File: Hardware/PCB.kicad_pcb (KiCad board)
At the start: 2 copper layers, 53.4 x 22 mm, 11 parts, among them J1 Conn_01x04_Pin, U1 ME54BS01_V1.0, U2 MCP1700x-330xxTO

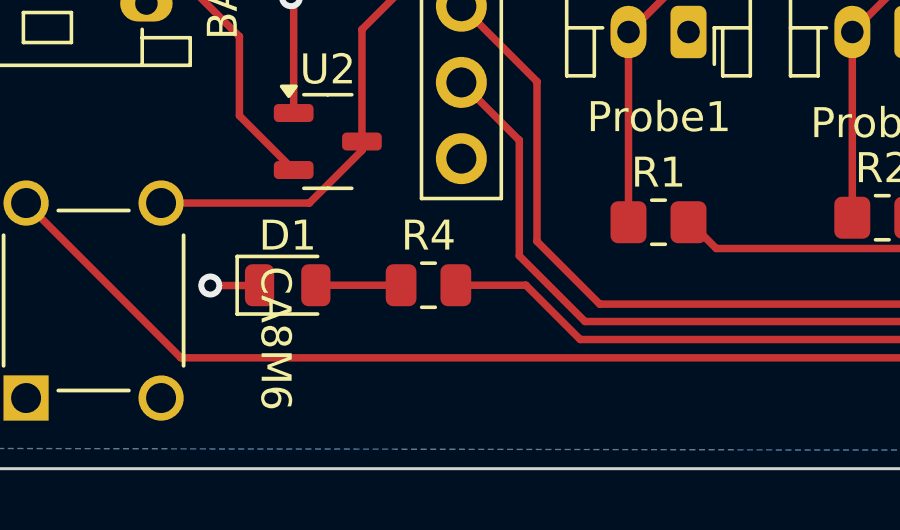
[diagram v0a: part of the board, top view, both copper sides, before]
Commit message: WIP Reworking schematic with Reddit feedback
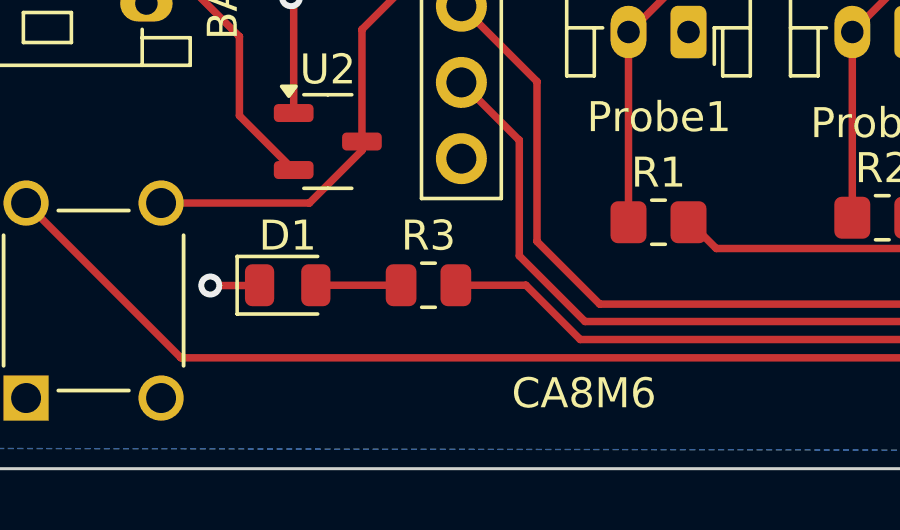
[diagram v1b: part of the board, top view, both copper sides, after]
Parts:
- renumbered R4 to R3
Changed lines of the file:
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@@
 	(paper "A4")
 	(title_block
-		(title "XIAO nRF52840 Dual Sensor")
-		(rev "4")
+		(title "Matter nRF54L15 Dual Temperature Sensor")
+		(rev "1")
 		(company "Cold Bear Ltd")
+		(comment 4 "AISLER Project ID: CJCXXZRD")
 	)
 	(layers
@@
 		(descr "Resistor SMD 0805 (2012 Metric), square (rectangular) end terminal, IPC_7351 nominal, (Body size source: IPC-SM-782 page 72, https://www.pcb-3d.com/wordpress/wp-content/uploads/ipc-sm-782a_amendment_1_and_2.pdf), generated with kicad-footprint-generator")
 		(tags "resistor")
-		(property "Reference" "R4"
+		(property "Reference" "R3"
 			(at 0 -1.65 0)
 			(layer "F.SilkS")
@@
 	)
 	(gr_text "CA8M6"
-		(at 51.68 75.34 270)
+		(at 64.96 75.34 0)
 		(layer "F.SilkS")
 		(effects

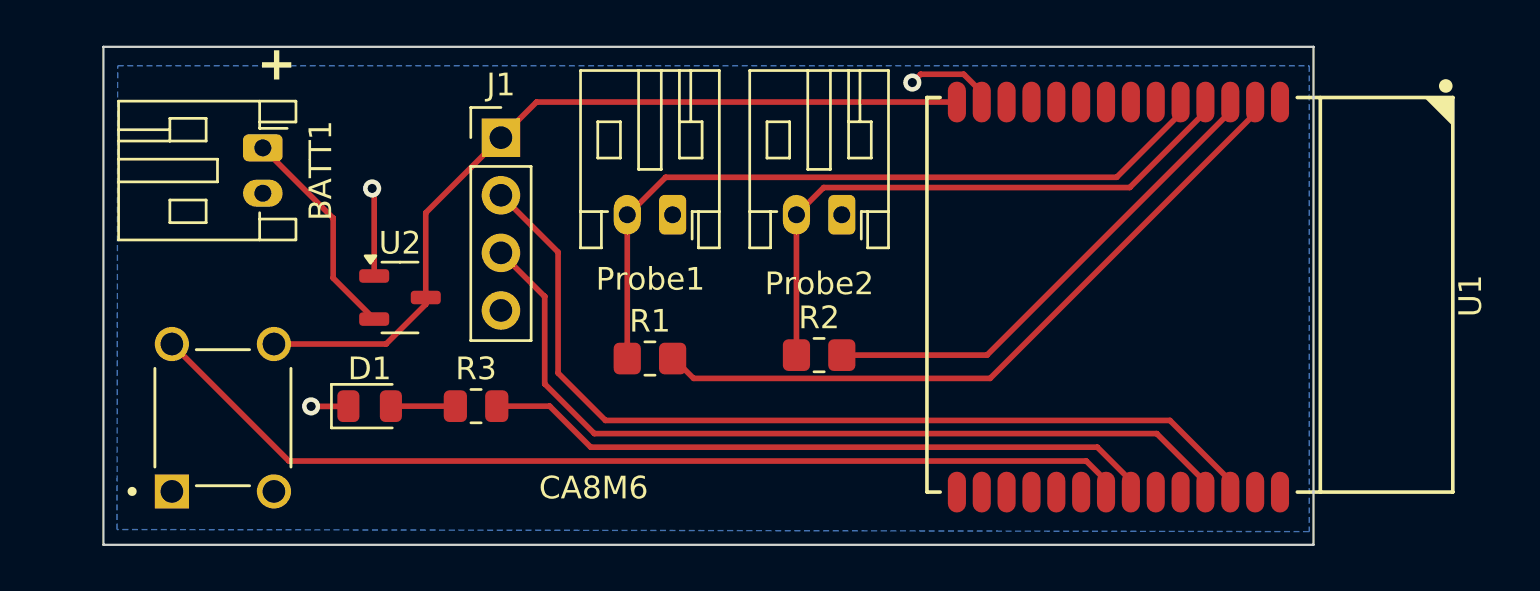
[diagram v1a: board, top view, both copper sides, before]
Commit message: Cleaned up schematic to be all in one. Trying to get updated layout for PCB
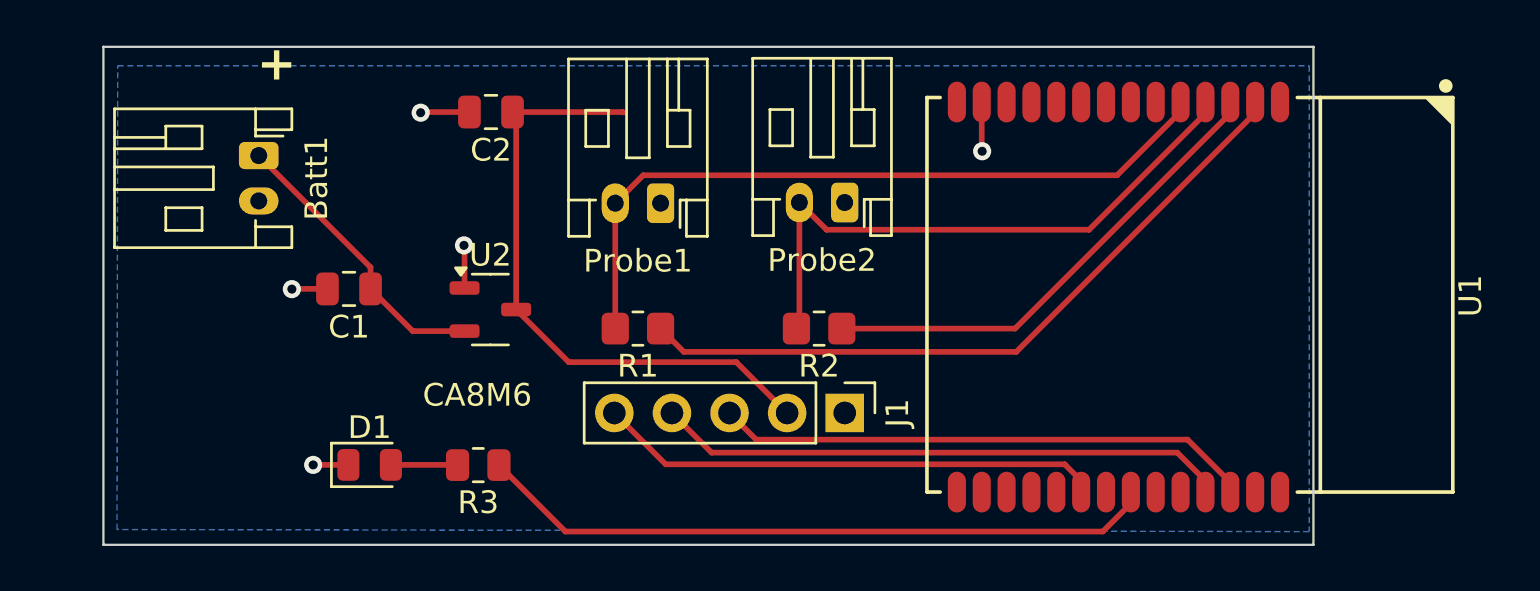
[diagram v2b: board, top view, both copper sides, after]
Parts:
- removed BATT1: Conn_01x02_Pin, Connector_JST:JST_PH_S2B-PH-K_1x02_P2.00mm_Horizontal
- removed S1: TS02-66-55-BK-100-LCR-D, TS02-66-55-BK-100-LCR-D:SW_TS02-66-55-BK-100-LCR-D
- added Batt1: Conn_01x02, Connector_JST:JST_PH_S2B-PH-K_1x02_P2.00mm_Horizontal, F.Cu at (47.8, 60.1)
- added C1: 1µF, Capacitor_SMD:C_0805_2012Metric, F.Cu at (51.8, 66.0)
- added C2: 1µF, Capacitor_SMD:C_0805_2012Metric, F.Cu at (58.0, 58.2)
- J1: value Conn_01x04_Pin -> Conn_01x05; footprint Connector_PinHeader_2.54mm:PinHeader_1x04_P2.54mm_Vertical -> Connector_PinHeader_2.54mm:PinHeader_1x05_P2.54mm_Vertical
- Probe1, Probe2: value Conn_01x02_Pin -> Conn_01x02
- R3: value R -> 50
- moved J1 19.4 mm to (73.6, 71.5), turned to -90 degrees
- moved U2 4.02 mm to (58.0, 66.9)
- moved R3 2.60 mm to (57.5, 73.8), turned to 180 degrees
- moved D1 2.59 mm to (52.7, 73.7)
- moved R1 1.42 mm to (64.5, 67.7), turned to 180 degrees
- moved R2 1.17 mm to (72.5, 67.7), turned to 180 degrees
- moved Probe1 0.74 mm to (65.5, 62.2)
- moved Probe2 0.56 mm to (73.6, 62.2)
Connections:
- J1 pad 1: /+3.3V -> GND
- J1 pad 2: /SWDCLK -> Net-(J1-Pin_2)
- J1 pad 3: /SWDIO -> Net-(J1-Pin_3)
- J1 pad 4: GND -> Net-(J1-Pin_4)
- Probe1 pad 2: /p1reading -> Net-(Probe1-Pin_2)
- Probe2 pad 2: /p2reading -> Net-(Probe2-Pin_2)
- R1 pad 1: /p1reading -> Net-(U1-P1.09)
- R1 pad 2: /dividerPower1 -> Net-(Probe1-Pin_2)
- R2 pad 1: /p2reading -> Net-(U1-P1.10)
- R2 pad 2: /dividerPower2 -> Net-(Probe2-Pin_2)
- R3 pad 1: Net-(D1-A) -> Net-(U1-P2.10)
- R3 pad 2: /indicator -> Net-(D1-A)
- U1 pad 14: /+3.3V -> Net-(J1-Pin_2)
- U1 pad 2: /dividerPower1 -> Net-(U1-P1.09)
- U1 pad 20: unconnected-(U1-NRESET-Pad20) -> Net-(J1-Pin_5)
- U1 pad 21: /reset -> Net-(U1-P2.09)
- U1 pad 22: /indicator -> Net-(U1-P2.10)
- U1 pad 25: /SWDIO -> Net-(J1-Pin_4)
- U1 pad 26: /SWDCLK -> Net-(J1-Pin_3)
- U1 pad 3: /dividerPower2 -> Net-(U1-P1.10)
- U1 pad 4: /p2reading -> Net-(Probe2-Pin_2)
- U1 pad 5: /p1reading -> Net-(Probe1-Pin_2)
- U2 pad 2: +BATT -> Net-(Batt1-Pin_1)
- U2 pad 3: /+3.3V -> Net-(J1-Pin_2)
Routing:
- net /reset: track 44.2 -> 0.00 mm
- net /SWDCLK: track 41.0 -> 0.00 mm
- net /SWDIO: track 38.4 -> 0.00 mm
- net /+3.3V: track 36.9 -> 0.00 mm
- net /p1reading: track 33.1 -> 0.00 mm
- net Net-(Probe1-Pin_2): track 0.00 -> 33.1 mm
- net Net-(U1-P1.09): track 0.00 -> 32.0 mm
- net /dividerPower1: track 31.3 -> 0.00 mm
- net Net-(U1-P2.10): track 0.00 -> 30.6 mm
- net /indicator: track 29.8 -> 0.00 mm
- net Net-(J1-Pin_2): track 0.00 -> 27.5 mm
- net Net-(Probe2-Pin_2): track 0.00 -> 26.6 mm
- net /p2reading: track 26.5 -> 0.00 mm
- net Net-(J1-Pin_4): track 0.00 -> 25.8 mm
- net Net-(J1-Pin_3): track 0.00 -> 24.3 mm
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
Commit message: Another PCB update
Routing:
- net Net-(J1-Pin_2): track 27.5 -> 42.4 mm
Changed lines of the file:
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@@
 	)
 	(segment
-		(start 59.13 66.89)
-		(end 61.447 69.207)
+		(start 69.04 69.41)
+		(end 71.08 71.45)
+		(width 0.25)
+		(layer "F.Cu")
+		(net 2)
+	)
+	(segment
+		(start 61.65 69.41)
+		(end 69.04 69.41)
 		(width 0.25)
 		(layer "F.Cu")
@@
 	)
 	(segment
-		(start 63.83 58.18)
-		(end 63.85 58.2)
-		(width 0.25)
-		(layer "F.Cu")
-		(net 2)
-	)
-	(segment
-		(start 58.97 58.18)
-		(end 63.83 58.18)
-		(width 0.25)
-		(layer "F.Cu")
-		(net 2)
-	)
-	(segment
 		(start 59.13 58.34)
 		(end 58.97 58.18)
@@
 	)
 	(segment
-		(start 68.837 69.207)
-		(end 71.08 71.45)
+		(start 59.13 66.89)
+		(end 61.65 69.41)
 		(width 0.25)
 		(layer "F.Cu")
@@
 	)
 	(segment
-		(start 61.447 69.207)
-		(end 68.837 69.207)
+		(start 78.566 57.74)
+		(end 59.41 57.74)
 		(width 0.25)
 		(layer "F.Cu")
+		(net 2)
+	)
+	(segment
+		(start 59.41 57.74)
+		(end 58.97 58.18)
+		(width 0.25)
+		(layer "F.Cu")

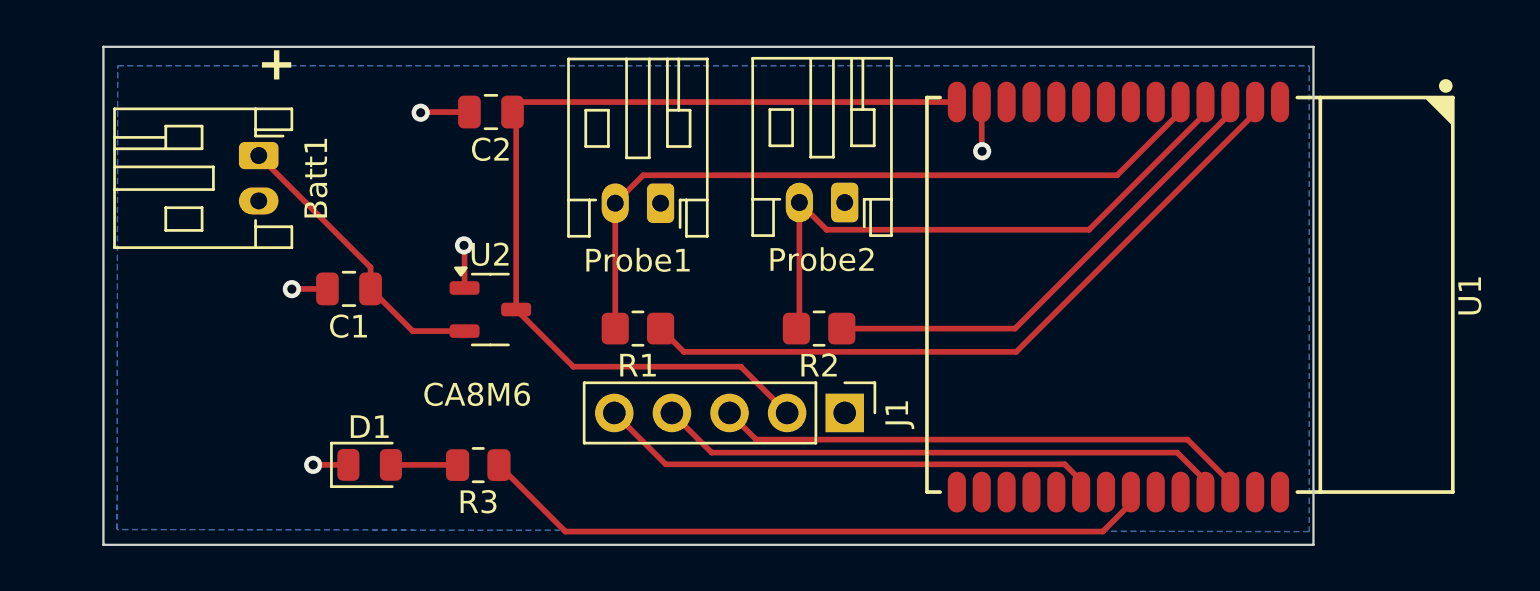
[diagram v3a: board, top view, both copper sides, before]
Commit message: PCB: Add another PIN to the header so power can be provided via J-Link.
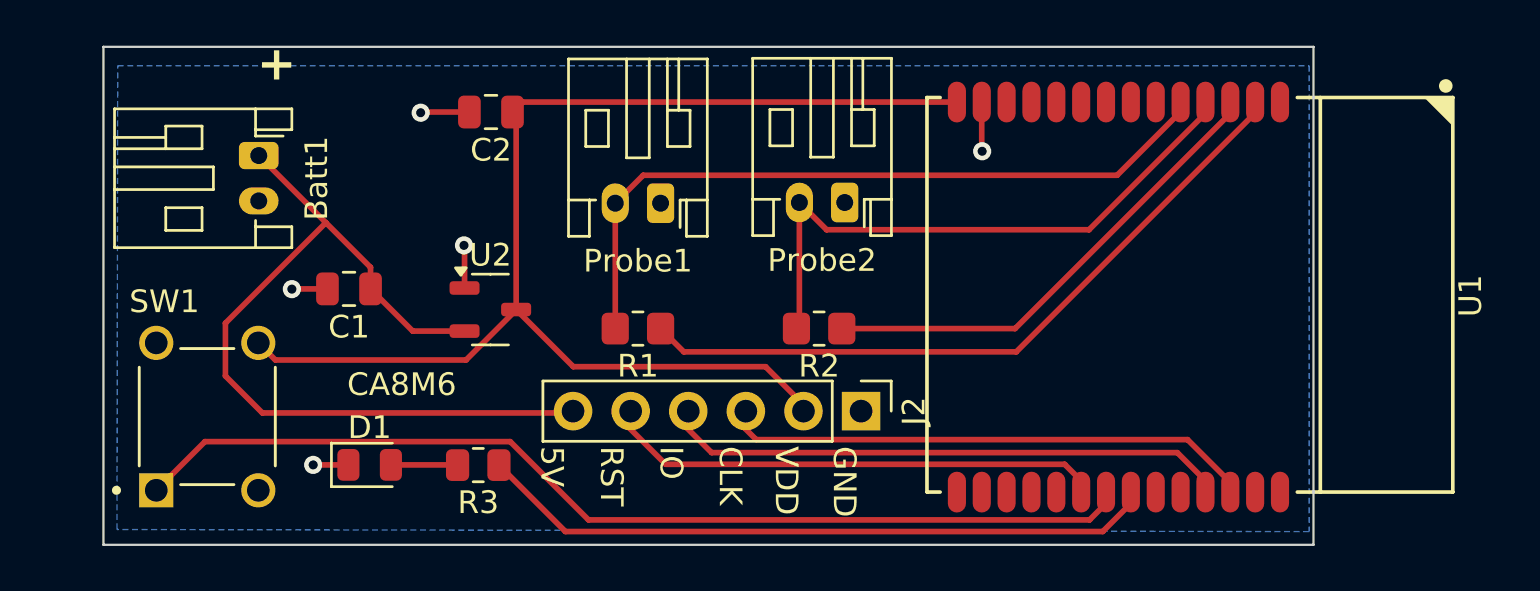
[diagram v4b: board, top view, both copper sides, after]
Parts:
- removed J1: Conn_01x05, Connector_PinHeader_2.54mm:PinHeader_1x05_P2.54mm_Vertical
- added J2: Conn_01x06, Connector_PinHeader_2.54mm:PinHeader_1x06_P2.54mm_Vertical, F.Cu at (74.3, 71.4)
- added SW1: SW_MEC_5E, TS02-66-55-BK-100-LCR-D:SW_TS02-66-55-BK-100-LCR-D, F.Cu at (45.5, 71.6)
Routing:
- net Net-(U1-P2.09): track 0.50 -> 45.5 mm
- net Net-(Batt1-Pin_1): track 12.8 -> 36.7 mm
- net Net-(J2-Pin_2): track 42.4 -> 55.9 mm
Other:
- board text added: "5V"
- board text added: "CLK"
- board text added: "GND"
- board text added: "IO"
- board text added: "RST"
- board text added: "VDD"

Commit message: Move decoupling capacitors closer to LDO. Ground module PIN 1.
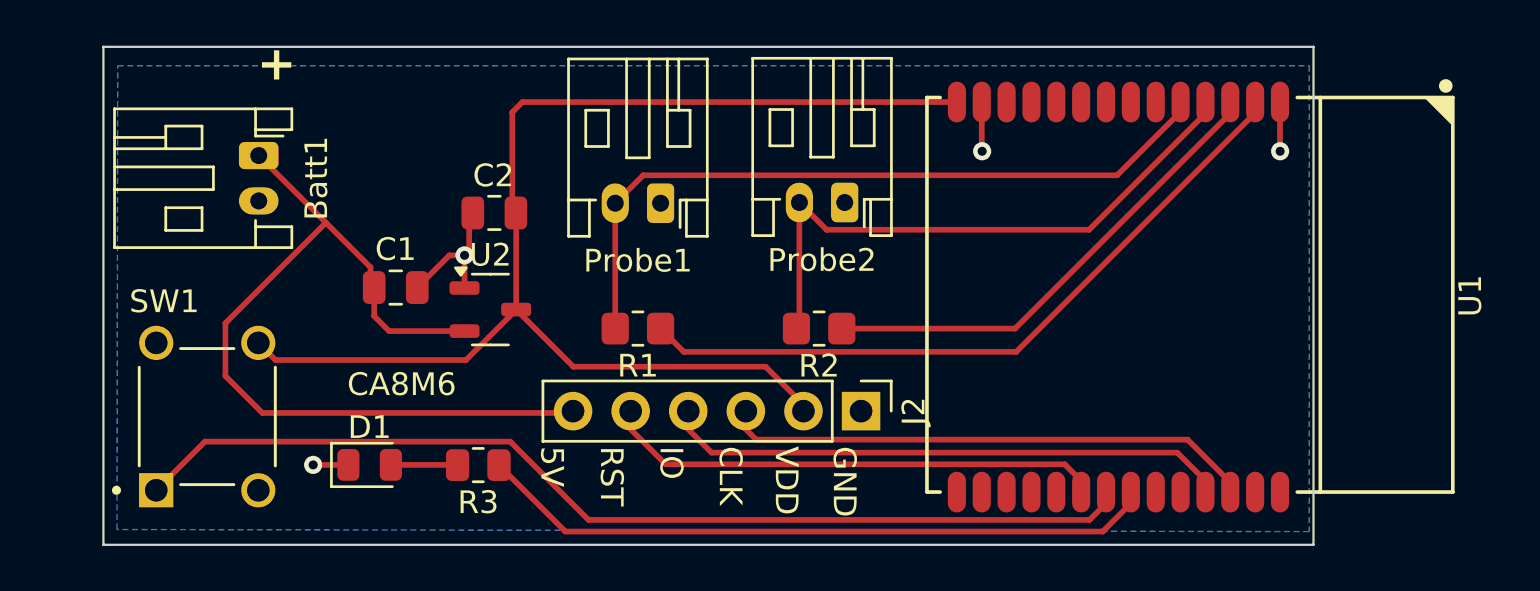
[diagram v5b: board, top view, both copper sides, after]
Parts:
- moved C2 4.45 mm to (58.2, 62.6)
- moved C1 2.06 mm to (53.8, 65.9), turned to 0 degrees
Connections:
- U1 pad 1: unconnected-(U1-GND-Pad1) -> GND
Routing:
- net GND: track 9.91 -> 12.6 mm, vias 5 -> 4
- net Net-(Batt1-Pin_1): track 36.7 -> 37.3 mm

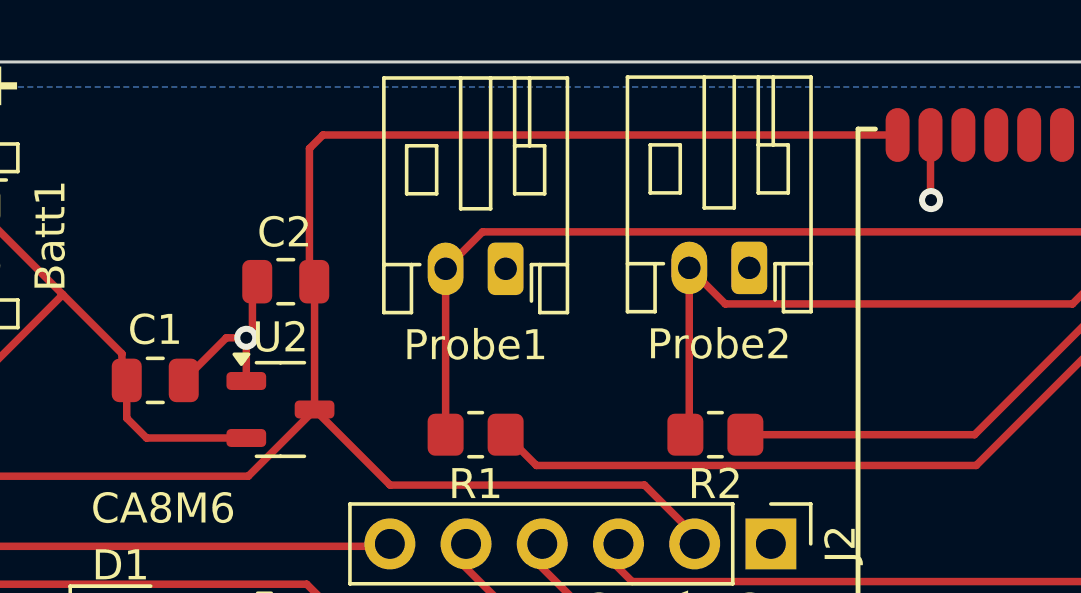
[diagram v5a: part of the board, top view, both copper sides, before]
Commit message: Move decoupling capacitors even closer
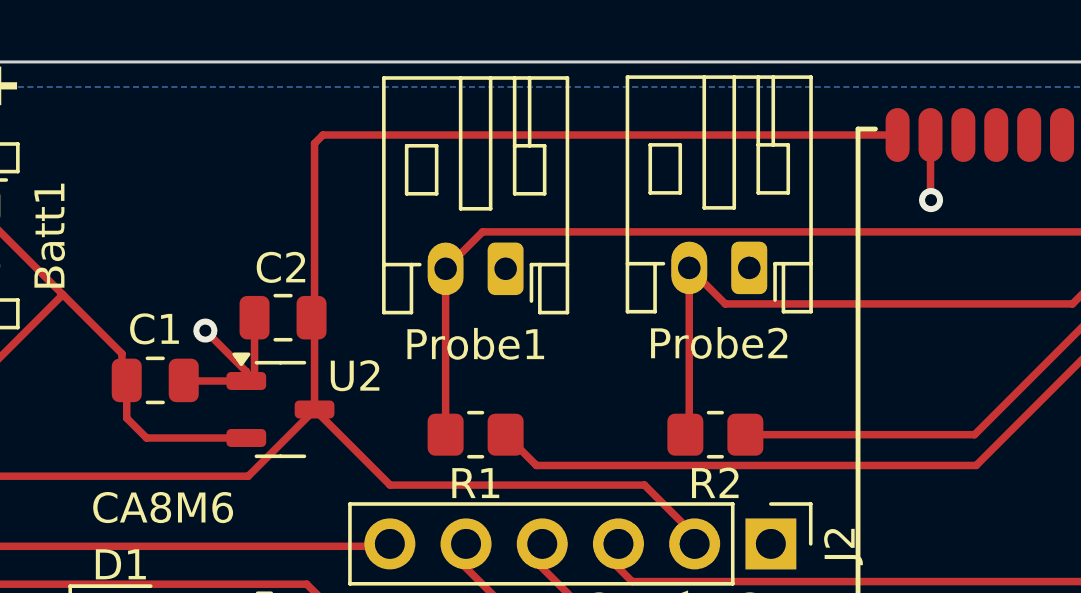
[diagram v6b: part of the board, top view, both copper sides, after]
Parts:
- moved C2 1.20 mm to (58.1, 63.8)
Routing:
- net GND: track 12.6 -> 13.1 mm
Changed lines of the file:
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@@
 		(tags "SOT TO_SOT_SMD")
 		(property "Reference" "U2"
-			(at 0 -2.4 0)
+			(at 2.4975 -1.09 0)
 			(layer "F.SilkS")
 			(effects
@@
 	(footprint "Capacitor_SMD:C_0805_2012Metric"
 		(layer "F.Cu")
-		(at 58.17 62.63 180)
+		(at 58.08 63.83 180)
 		(descr "Capacitor SMD 0805 (2012 Metric), square (rectangular) end terminal, IPC_7351 nominal, (Body size source: IPC-SM-782 page 76, https://www.pcb-3d.com/wordpress/wp-content/uploads/ipc-sm-782a_amendment_1_and_2.pdf, https://docs.google.com/spreadsheets/d/1BsfQQcO9C6DZCsRaXUlFlo91Tg2WpOkGARC1WS5S8t0/edit?usp=sharing), generated with kicad-footprint-generator")
 		(tags "capacitor")
@@
 	)
 	(segment
-		(start 54.77 65.92)
-		(end 56.19 64.5)
-		(width 0.25)
-		(layer "F.Cu")
-		(net 1)
-	)
-	(segment
-		(start 56.19 64.5)
-		(end 56.855 64.5)
-		(width 0.25)
-		(layer "F.Cu")
-		(net 1)
-	)
-	(segment
 		(start 92.814 59.904)
 		(end 92.82 59.91)
@@
 	)
 	(segment
-		(start 56.855 64.5)
+		(start 57.13 65.665)
 		(end 56.855 65.94)
 		(width 0.25)
@@
 	)
 	(segment
+		(start 57.06 63.9)
+		(end 57.13 63.83)
+		(width 0.25)
+		(layer "F.Cu")
+		(net 1)
+	)
+	(segment
+		(start 56.855 65.94)
+		(end 54.79 65.94)
+		(width 0.25)
+		(layer "F.Cu")
+		(net 1)
+	)
+	(segment
+		(start 57.13 63.83)
+		(end 57.13 65.665)
+		(width 0.25)
+		(layer "F.Cu")
+		(net 1)
+	)
+	(segment
 		(start 79.662 57.74)
 		(end 79.662 59.892)
@@
 	)
 	(segment
-		(start 57.06 64.295)
-		(end 56.855 64.5)
+		(start 55.49 64.26)
+		(end 56.855 65.625)
 		(width 0.25)
 		(layer "F.Cu")
@@
 	)
 	(segment
-		(start 57.06 62.6)
-		(end 57.06 64.295)
+		(start 54.79 65.94)
+		(end 54.77 65.92)
 		(width 0.25)
 		(layer "F.Cu")
@@
 		(net 1)
 	)
+	(segment
+		(start 56.855 65.625)
+		(end 56.855 65.94)
+		(width 0.25)
+		(layer "F.Cu")
+		(net 1)
+	)
 	(via
-		(at 56.855 64.5)
+		(at 55.49 64.26)
 		(size 0.8)
 		(drill 0.4)
@@
 	)
 	(segment
-		(start 59.13 62.77)
-		(end 58.96 62.6)
-		(width 0.25)
-		(layer "F.Cu")
-		(net 28)
-	)
-	(segment
 		(start 71.8 71.08)
 		(end 71.8 71.37)
@@
 	)
 	(segment
+		(start 59.13 58.02)
+		(end 59.41 57.74)
+		(width 0.25)
+		(layer "F.Cu")
+		(net 28)
+	)
+	(segment
 		(start 70.13 69.41)
 		(end 71.8 71.08)
@@
 	(segment
 		(start 59.13 66.89)
-		(end 59.13 62.77)
+		(end 59.13 66.904822)
 		(width 0.25)
 		(layer "F.Cu")
@@
 	)
 	(segment
-		(start 58.96 58.19)
-		(end 59.41 57.74)
+		(start 59.13 66.89)
+		(end 59.13 58.02)
 		(width 0.25)
 		(layer "F.Cu")
@@
 	)
 	(segment
-		(start 78.566 57.74)
-		(end 59.41 57.74)
-		(width 0.25)
-		(layer "F.Cu")
-		(net 28)
-	)
-	(segment
-		(start 59.13 66.89)
-		(end 59.13 66.904822)
-		(width 0.25)
-		(layer "F.Cu")
-		(net 28)
-	)
-	(segment
-		(start 58.96 62.6)
-		(end 58.96 58.19)
-		(width 0.25)
-		(layer "F.Cu")
+		(start 59.41 57.74)
+		(end 78.566 57.74)
+		(width 0.25)
+		(layer "F.Cu")
